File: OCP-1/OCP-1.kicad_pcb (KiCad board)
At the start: 2 copper layers, 45 x 40 mm, 50 parts, among them K1 Кнопка_KLS7-TS5401-1.35-250-T, K2 Кнопка_KLS7-TS5401-1.35-250-T, K3 Кнопка_KLS7-TS5401-1.35-250-T, K4 Кнопка_KLS7-TS5401-1.35-250-T, X1 Клеммник_х2

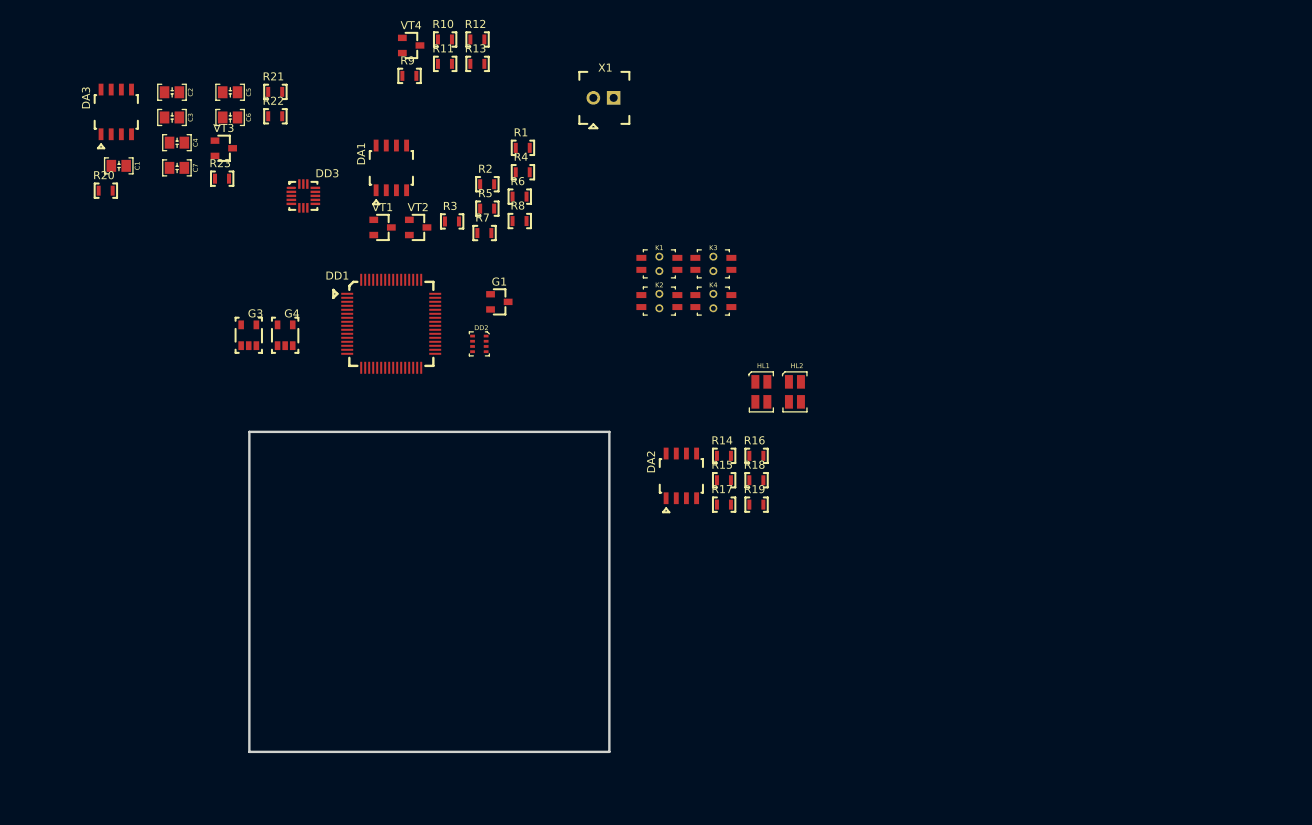
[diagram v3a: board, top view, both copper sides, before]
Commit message: добавлена схема включения и расположение индикаторов
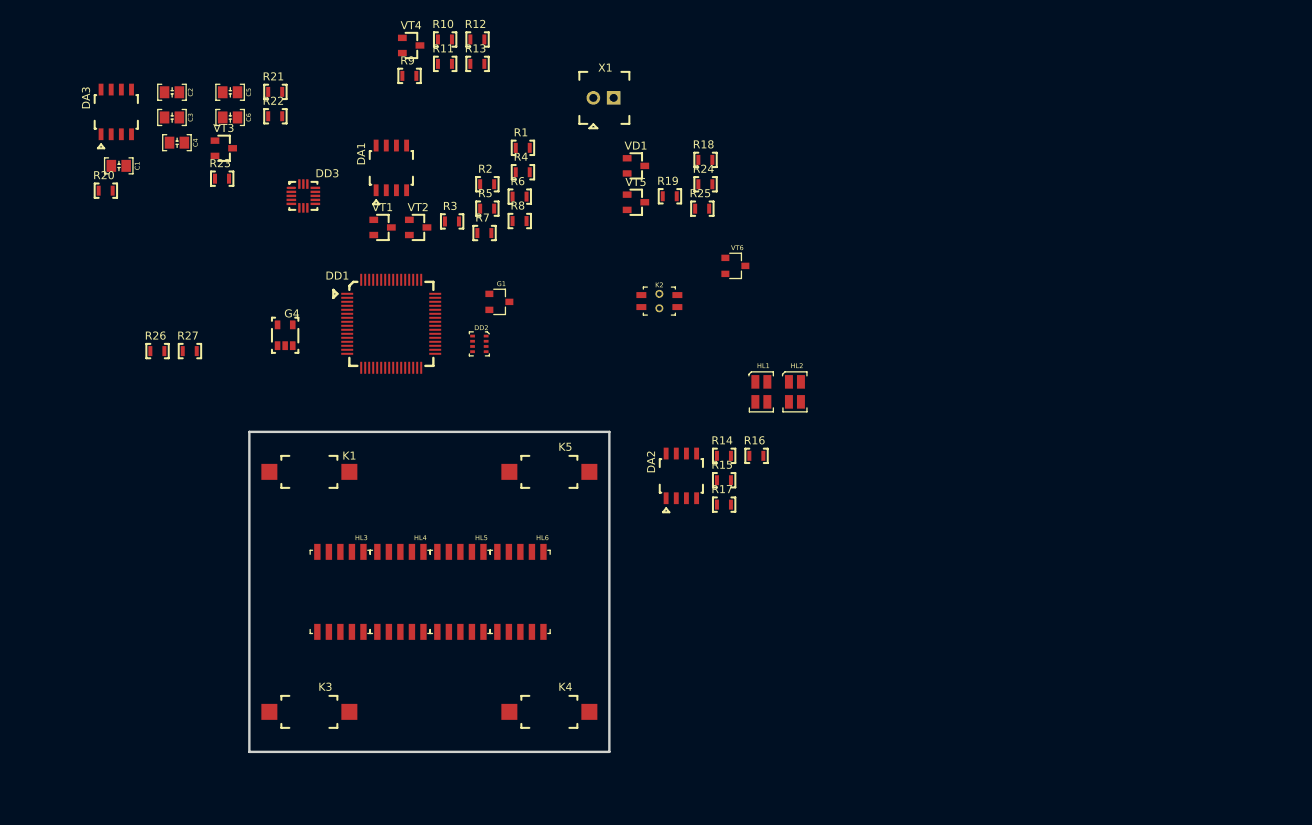
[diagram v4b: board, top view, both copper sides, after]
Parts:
- removed C7: Конденсатор_керамический, N_RLC:Конденсатор_SMD_IEC_0805
- removed G3: LDO_TPS76325DBVR, N_G:Преобразователь_LM2703_SOT-23-5
- added HL3: Индикатор_7сегм_TOS-F2101AMG, N_VD_HL:LED-7SEGM-10x6,9, F.Cu at (86.5, 120.0)
- added HL4: Индикатор_7сегм_TOS-F2101AMG, N_VD_HL:LED-7SEGM-10x6,9, F.Cu at (94.0, 120.0)
- added HL5: Индикатор_7сегм_TOS-F2101AMG, N_VD_HL:LED-7SEGM-10x6,9, F.Cu at (101.5, 120.0)
- added HL6: Индикатор_7сегм_TOS-F2101AMG, N_VD_HL:LED-7SEGM-10x6,9, F.Cu at (109.0, 120.0)
- added K5: кнопка, N_X:Кнопка_FSMSM, F.Cu at (107.5, 105.0)
- added R24: Резистор_0,065Вт, N_RLC:Резистор_SMD_0603_0,065_Вт, F.Cu at (132.0, 69.0)
- added R25: Резистор_0,065Вт, N_RLC:Резистор_SMD_0603_0,065_Вт, F.Cu at (131.6, 72.1)
- added R26: Резистор_0,065Вт, N_RLC:Резистор_SMD_0603_0,065_Вт, F.Cu at (63.5, 89.9)
- added R27: Резистор_0,065Вт, N_RLC:Резистор_SMD_0603_0,065_Вт, F.Cu at (67.6, 89.9)
- added VD1: Диоды_шоттки_BAR43CFILM, N_VD_HL:Транзистор_IRLML6344TR_SOT-23, F.Cu at (123.3, 66.8)
- added VT5: Транзистор_полевой_P-канал(IRLML2246TRPBF), N_VD_HL:Транзистор_IRLML6344TR_SOT-23, F.Cu at (123.3, 71.3)
- added VT6: Транзистор_полевой_N-канальный_КП526А9, MOTOR_VD_VT_HL:Корпус_КТ-46, F.Cu at (135.8, 79.2)
- G1: footprint N_VD_HL:Транзистор_IRLML6344TR_SOT-23 -> MOTOR_VD_VT_HL:Корпус_КТ-46
- K1, K3, K4: value Кнопка_KLS7-TS5401-1.35-250-T -> кнопка; footprint N_X:Кнопка_KLS7-TS5401 -> N_X:Кнопка_FSMSM
- moved K3 76.7 mm to (77.5, 135.0)
- moved K4 55.7 mm to (107.5, 135.0)
- moved K1 52.9 mm to (77.5, 105.0)
- moved R18 40.5 mm to (132.0, 66.0)
- moved R19 40.0 mm to (127.5, 70.5)
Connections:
- net /2V5.FB1 renamed /1V5.FB1
- net Net-(K1-Pad2) renamed /B-UP
- net Net-(K3-Pad2) renamed /B-DOWN
- net Net-(K4-Pad2) renamed /B-BACK
- DA1 pad 2: /2V5.REF -> /1V225.REF
- G1 pad 1: /2V5.REF -> /2V5
- K1 pad 1: Net-(K1-Pad1) -> /GND
- K2 pad 1: Net-(K2-Pad1) -> /RES
- K2 pad 2: Net-(K2-Pad2) -> /GND
- K2 pad 3: Net-(K2-Pad3) -> /RES
- K2 pad 4: Net-(K2-Pad4) -> /GND
- K3 pad 1: Net-(K3-Pad1) -> /GND
- K4 pad 1: Net-(K4-Pad1) -> /GND
- R18 pad 1: /2V5.REF -> Net-(R18-Pad1)
- R18 pad 2: /1V5.REF -> /4V1.OUT
- R19 pad 1: /1V5.REF -> Net-(R19-Pad1)
- R20 pad 1: /4V1.OUT -> Net-(R20-Pad1)
- R9 pad 2: /2V5.REF -> /2V5
- VT3 pad 2: /4V1.OUT -> Net-(R20-Pad1)

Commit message: заготовка usb-type-c
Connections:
- DA1 pad 2: /1V225.REF -> (no net)
- DA1 pad 6: /1V5.REF -> (no net)
- DA3 pad 5: Net-(DA3-Pad5) -> (no net)
- DA3 pad 6: Net-(DA3-Pad6) -> (no net)
- DA3 pad 7: Net-(DA3-Pad7) -> (no net)
- DD1 pad 1: Net-(DD1-Pad1) -> (no net)
- DD1 pad 10: Net-(DD1-Pad10) -> (no net)
- DD1 pad 11: Net-(DD1-Pad11) -> (no net)
- DD1 pad 12: Net-(DD1-Pad12) -> (no net)
- DD1 pad 13: Net-(DD1-Pad13) -> (no net)
- DD1 pad 14: Net-(DD1-Pad14) -> (no net)
- DD1 pad 15: Net-(DD1-Pad15) -> (no net)
- DD1 pad 16: Net-(DD1-Pad16) -> (no net)
- DD1 pad 17: Net-(DD1-Pad17) -> (no net)
- DD1 pad 18: Net-(DD1-Pad18) -> (no net)
- DD1 pad 19: Net-(DD1-Pad19) -> (no net)
- DD1 pad 2: Net-(DD1-Pad2) -> (no net)
- DD1 pad 20: Net-(DD1-Pad20) -> (no net)
- DD1 pad 21: Net-(DD1-Pad21) -> (no net)
- DD1 pad 22: Net-(DD1-Pad22) -> (no net)
- DD1 pad 23: Net-(DD1-Pad23) -> (no net)
- DD1 pad 24: Net-(DD1-Pad24) -> (no net)
- DD1 pad 25: Net-(DD1-Pad25) -> (no net)
- DD1 pad 26: Net-(DD1-Pad26) -> (no net)
- DD1 pad 27: Net-(DD1-Pad27) -> (no net)
- DD1 pad 28: Net-(DD1-Pad28) -> (no net)
- DD1 pad 29: Net-(DD1-Pad29) -> (no net)
- DD1 pad 3: Net-(DD1-Pad3) -> (no net)
- DD1 pad 30: Net-(DD1-Pad30) -> (no net)
- DD1 pad 31: Net-(DD1-Pad31) -> (no net)
- DD1 pad 32: Net-(DD1-Pad32) -> (no net)
- DD1 pad 33: Net-(DD1-Pad33) -> (no net)
- DD1 pad 34: Net-(DD1-Pad34) -> (no net)
- DD1 pad 35: Net-(DD1-Pad35) -> (no net)
- DD1 pad 36: Net-(DD1-Pad36) -> (no net)
- DD1 pad 37: Net-(DD1-Pad37) -> (no net)
- DD1 pad 38: Net-(DD1-Pad38) -> (no net)
- DD1 pad 39: Net-(DD1-Pad39) -> (no net)
- DD1 pad 4: Net-(DD1-Pad4) -> (no net)
- DD1 pad 40: Net-(DD1-Pad40) -> (no net)
- DD1 pad 41: Net-(DD1-Pad41) -> (no net)
- DD1 pad 42: Net-(DD1-Pad42) -> (no net)
- DD1 pad 43: Net-(DD1-Pad43) -> (no net)
- DD1 pad 44: Net-(DD1-Pad44) -> (no net)
- DD1 pad 45: Net-(DD1-Pad45) -> (no net)
- DD1 pad 46: Net-(DD1-Pad46) -> (no net)
- DD1 pad 47: Net-(DD1-Pad47) -> (no net)
- DD1 pad 48: Net-(DD1-Pad48) -> (no net)
- DD1 pad 49: Net-(DD1-Pad49) -> (no net)
- DD1 pad 5: Net-(DD1-Pad5) -> (no net)
- DD1 pad 50: Net-(DD1-Pad50) -> (no net)
- DD1 pad 51: Net-(DD1-Pad51) -> (no net)
- DD1 pad 52: Net-(DD1-Pad52) -> (no net)
- DD1 pad 53: Net-(DD1-Pad53) -> (no net)
- DD1 pad 54: Net-(DD1-Pad54) -> (no net)
- DD1 pad 55: Net-(DD1-Pad55) -> (no net)
- DD1 pad 56: Net-(DD1-Pad56) -> (no net)
- DD1 pad 57: Net-(DD1-Pad57) -> (no net)
- DD1 pad 58: Net-(DD1-Pad58) -> (no net)
- DD1 pad 59: Net-(DD1-Pad59) -> (no net)
- DD1 pad 6: Net-(DD1-Pad6) -> (no net)
- DD1 pad 60: Net-(DD1-Pad60) -> (no net)
- DD1 pad 61: Net-(DD1-Pad61) -> (no net)
- DD1 pad 62: Net-(DD1-Pad62) -> (no net)
- DD1 pad 63: Net-(DD1-Pad63) -> (no net)
- DD1 pad 64: Net-(DD1-Pad64) -> (no net)
- DD1 pad 7: Net-(DD1-Pad7) -> (no net)
- DD1 pad 8: Net-(DD1-Pad8) -> (no net)
- DD1 pad 9: Net-(DD1-Pad9) -> (no net)
- DD2 pad 1: Net-(DD2-Pad1) -> (no net)
- DD2 pad 2: Net-(DD2-Pad2) -> (no net)
- DD2 pad 3: Net-(DD2-Pad3) -> (no net)
- DD2 pad 4: Net-(DD2-Pad4) -> (no net)
- DD2 pad 5: Net-(DD2-Pad5) -> (no net)
- DD2 pad 6: Net-(DD2-Pad6) -> (no net)
- DD2 pad 7: Net-(DD2-Pad7) -> (no net)
- DD2 pad 8: Net-(DD2-Pad8) -> (no net)
- DD3 pad 1: Net-(DD3-Pad1) -> (no net)
- DD3 pad 10: Net-(DD3-Pad10) -> (no net)
- DD3 pad 11: Net-(DD3-Pad11) -> (no net)
- DD3 pad 12: Net-(DD3-Pad12) -> (no net)
- DD3 pad 13: Net-(DD3-Pad13) -> (no net)
- DD3 pad 14: Net-(DD3-Pad14) -> (no net)
- DD3 pad 15: Net-(DD3-Pad15) -> (no net)
- DD3 pad 16: Net-(DD3-Pad16) -> (no net)
- DD3 pad 2: Net-(DD3-Pad2) -> (no net)
- DD3 pad 3: Net-(DD3-Pad3) -> (no net)
- DD3 pad 4: Net-(DD3-Pad4) -> (no net)
- DD3 pad 5: Net-(DD3-Pad5) -> (no net)
- DD3 pad 6: Net-(DD3-Pad6) -> (no net)
- DD3 pad 7: Net-(DD3-Pad7) -> (no net)
- DD3 pad 8: Net-(DD3-Pad8) -> (no net)
- DD3 pad 9: Net-(DD3-Pad9) -> (no net)
- G1 pad 3: Net-(G1-Pad3) -> (no net)
- G4 pad 4: Net-(G4-Pad4) -> (no net)
- HL1 pad 1: Net-(HL1-Pad1) -> (no net)
- HL1 pad 2: Net-(HL1-Pad2) -> (no net)
- HL1 pad 3: Net-(HL1-Pad3) -> (no net)
- HL1 pad 4: Net-(HL1-Pad4) -> (no net)
- HL2 pad 1: Net-(HL2-Pad1) -> (no net)
- HL2 pad 2: Net-(HL2-Pad2) -> (no net)
- HL2 pad 3: Net-(HL2-Pad3) -> (no net)
- HL2 pad 4: Net-(HL2-Pad4) -> (no net)
- HL3 pad 1: Net-(HL3-Pad1) -> (no net)
- HL3 pad 10: Net-(HL3-Pad10) -> (no net)
- HL3 pad 2: Net-(HL3-Pad2) -> (no net)
- HL3 pad 3: Net-(HL3-Pad3) -> (no net)
- HL3 pad 4: Net-(HL3-Pad4) -> (no net)
- HL3 pad 5: Net-(HL3-Pad5) -> (no net)
- HL3 pad 6: Net-(HL3-Pad6) -> (no net)
- HL3 pad 7: Net-(HL3-Pad7) -> (no net)
- HL3 pad 8: Net-(HL3-Pad8) -> (no net)
- HL3 pad 9: Net-(HL3-Pad9) -> (no net)
- HL4 pad 1: Net-(HL4-Pad1) -> (no net)
- HL4 pad 10: Net-(HL4-Pad10) -> (no net)
- HL4 pad 2: Net-(HL4-Pad2) -> (no net)
- HL4 pad 3: Net-(HL4-Pad3) -> (no net)
- HL4 pad 4: Net-(HL4-Pad4) -> (no net)
- HL4 pad 5: Net-(HL4-Pad5) -> (no net)
- HL4 pad 6: Net-(HL4-Pad6) -> (no net)
- HL4 pad 7: Net-(HL4-Pad7) -> (no net)
- HL4 pad 8: Net-(HL4-Pad8) -> (no net)
- HL4 pad 9: Net-(HL4-Pad9) -> (no net)
- HL5 pad 1: Net-(HL5-Pad1) -> (no net)
- HL5 pad 10: Net-(HL5-Pad10) -> (no net)
- HL5 pad 2: Net-(HL5-Pad2) -> (no net)
- HL5 pad 3: Net-(HL5-Pad3) -> (no net)
- HL5 pad 4: Net-(HL5-Pad4) -> (no net)
- HL5 pad 5: Net-(HL5-Pad5) -> (no net)
- HL5 pad 6: Net-(HL5-Pad6) -> (no net)
- HL5 pad 7: Net-(HL5-Pad7) -> (no net)
- HL5 pad 8: Net-(HL5-Pad8) -> (no net)
- HL5 pad 9: Net-(HL5-Pad9) -> (no net)
- HL6 pad 1: Net-(HL6-Pad1) -> (no net)
- HL6 pad 10: Net-(HL6-Pad10) -> (no net)
- HL6 pad 2: Net-(HL6-Pad2) -> (no net)
- HL6 pad 3: Net-(HL6-Pad3) -> (no net)
- HL6 pad 4: Net-(HL6-Pad4) -> (no net)
- HL6 pad 5: Net-(HL6-Pad5) -> (no net)
- HL6 pad 6: Net-(HL6-Pad6) -> (no net)
- HL6 pad 7: Net-(HL6-Pad7) -> (no net)
- HL6 pad 8: Net-(HL6-Pad8) -> (no net)
- HL6 pad 9: Net-(HL6-Pad9) -> (no net)
- K1 pad 2: /B-UP -> (no net)
- K3 pad 2: /B-DOWN -> (no net)
- K4 pad 2: /B-BACK -> (no net)
- R24 pad 1: /SELF-TURN -> (no net)
- R25 pad 1: /SENS-B-PWR -> (no net)
- VT1 pad 3: /5V.IN -> (no net)
